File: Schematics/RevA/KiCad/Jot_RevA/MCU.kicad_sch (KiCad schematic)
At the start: 7 parts, among them U1 MDBT50Q-1MV2, Y1 32.768kHz

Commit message: Sensors sheet: U7 LIS2DW12 wired (I2C, SA0 high = 0x19, INT1 to ACC_INT1); clear wrong footprints on C6, C7, C10, C12, C13, Y1
Co-Authored-By: Claude Opus 5.5 <noreply@anthropic.com>
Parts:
- C6, C7: footprint Package_SO:SOIC-8_3.9x4.9mm_P1.27mm -> (none)
- Y1: footprint Relay_THT:Relay_SPDT_HsinDa_Y14 -> (none)
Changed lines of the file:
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@@
 		)
 		(property "Intersheetrefs" "${INTERSHEET_REFS}"
-			(at 111.76 134.62 0)
+			(at 100.0662 134.62 0)
 			(hide yes)
 			(show_name no)
@@
 			)
 		)
-		(property "Footprint" "Package_SO:SOIC-8_3.9x4.9mm_P1.27mm"
+		(property "Footprint" ""
 			(at 157.1752 39.37 0)
 			(hide yes)
@@
 			)
 		)
-		(property "Footprint" "Relay_THT:Relay_SPDT_HsinDa_Y14"
+		(property "Footprint" ""
 			(at 196.85 73.66 0)
 			(hide yes)
@@
 			)
 		)
-		(property "Footprint" "Package_SO:SOIC-8_3.9x4.9mm_P1.27mm"
+		(property "Footprint" ""
 			(at 130.5052 39.37 0)
 			(hide yes)

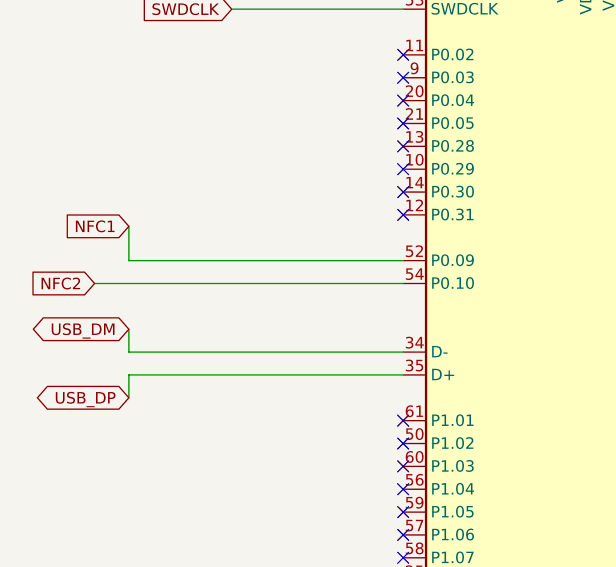
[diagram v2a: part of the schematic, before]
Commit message: NFC sheet: new sheet with NFC1/NFC2 labels and title block; title blocks restored after an editor overwrite; MCU NFC2 label tidied
Co-Authored-By: Claude Opus 5.5 <noreply@anthropic.com>
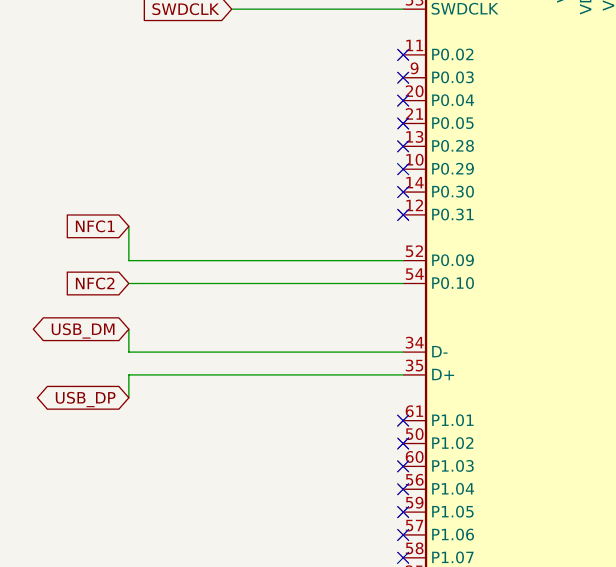
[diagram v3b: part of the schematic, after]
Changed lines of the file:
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@@
 	(wire
 		(pts
-			(xy 87.63 93.98) (xy 121.92 93.98)
+			(xy 91.44 93.98) (xy 121.92 93.98)
 		)
 		(stroke
@@
 	(global_label "NFC2"
 		(shape input)
-		(at 87.63 93.98 180)
-		(fields_autoplaced yes)
-		(effects
-			(font
-				(size 1.27 1.27)
-			)
-			(justify right)
-		)
-		(property "Intersheetrefs" "${INTERSHEET_REFS}"
-			(at 79.7462 93.98 0)
-			(hide yes)
-			(show_name no)
+		(at 91.44 93.98 180)
+		(fields_autoplaced yes)
+		(effects
+			(font
+				(size 1.27 1.27)
+			)
+			(justify right)
+		)
+		(property "Intersheetrefs" "${INTERSHEET_REFS}"
+			(at 83.5562 93.98 0)
+			(hide yes)
+			(show_name no)

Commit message: Footprints: all resistors (0402, R19 1206) and capacitors (0402, 10 uF 0603) assigned to match the BOM
Co-Authored-By: Claude Opus 5.5 <noreply@anthropic.com>
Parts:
- C6, C7: footprint (none) -> Capacitor_SMD:C_0603_1608Metric
- C8, C9: footprint (none) -> Capacitor_SMD:C_0402_1005Metric
- R14: footprint (none) -> Resistor_SMD:R_0402_1005Metric
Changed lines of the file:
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@@
 			)
 		)
-		(property "Footprint" ""
+		(property "Footprint" "Capacitor_SMD:C_0603_1608Metric"
 			(at 157.1752 39.37 0)
 			(hide yes)
@@
 			)
 		)
-		(property "Footprint" ""
+		(property "Footprint" "Capacitor_SMD:C_0402_1005Metric"
 			(at 191.4652 82.55 0)
 			(hide yes)
@@
 			)
 		)
-		(property "Footprint" ""
+		(property "Footprint" "Capacitor_SMD:C_0402_1005Metric"
 			(at 205.4352 82.55 0)
 			(hide yes)
@@
 			)
 		)
-		(property "Footprint" ""
+		(property "Footprint" "Capacitor_SMD:C_0603_1608Metric"
 			(at 130.5052 39.37 0)
 			(hide yes)
@@
 			)
 		)
-		(property "Footprint" ""
+		(property "Footprint" "Resistor_SMD:R_0402_1005Metric"
 			(at 163.83 29.972 90)
 			(hide yes)

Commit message: Footprints: D1 LED 0603, D4 SOD-123, Y1 3215 crystal
Co-Authored-By: Claude Opus 5.5 <noreply@anthropic.com>
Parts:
- Y1: footprint (none) -> Crystal:Crystal_SMD_3215-2Pin_3.2x1.5mm
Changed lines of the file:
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@@
 			)
 		)
-		(property "Footprint" ""
+		(property "Footprint" "Crystal:Crystal_SMD_3215-2Pin_3.2x1.5mm"
 			(at 196.85 73.66 0)
 			(hide yes)
